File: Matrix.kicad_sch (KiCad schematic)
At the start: 139 parts, among them K1 esc, K10 9, K11 0, K12 -, K13 =, K15 backspace, K16 macro1, K17 tab, K18 q, K19 w, K2 1, K20 e, K21 r, K22 t, K23 y, K24 u, K25 i, K26 o, K27 p, K28 [, K29 ], K3 2, K30 \, K31 macro 2, K32 Caps, K33 a, K34 s, K35 d, K36 f, K37 g, K38 h, K39 j, K4 3, K40 k, K41 l, K42 ;, K43 ', K44 enter, K45 macro 3, K46 shift, K47 z, K48 x, K49 c, K5 4, K50 v, K51 b, K52 fn, K53 n, K54 m, K55 ,, K56 ., K57 /, K58 shift right, K59 up, K6 5, K60 ctrl left, K61 alt right, K62 space left, K63 code, K64 space right, K65 ctrl right, K66 left, K67 down, K68 right, K69 split backspace, K7 6, K70 space left 2, K71 code 2, K8 7, K9 8

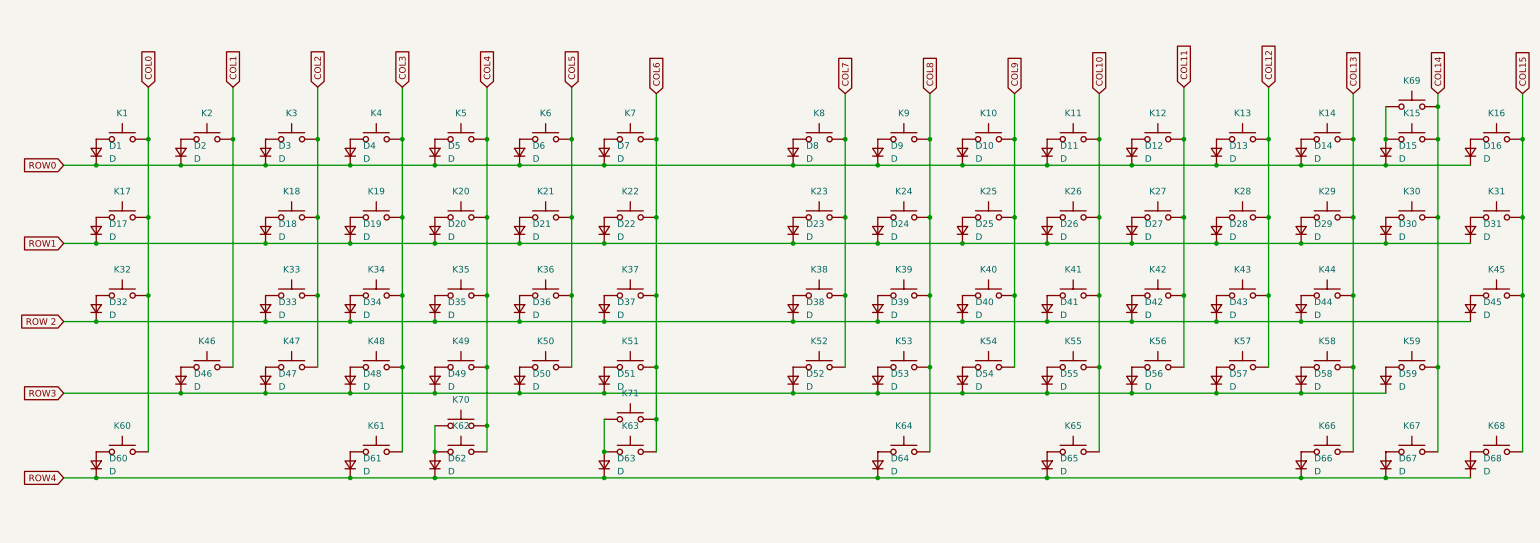
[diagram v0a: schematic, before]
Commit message: fixed footprint & Symbol
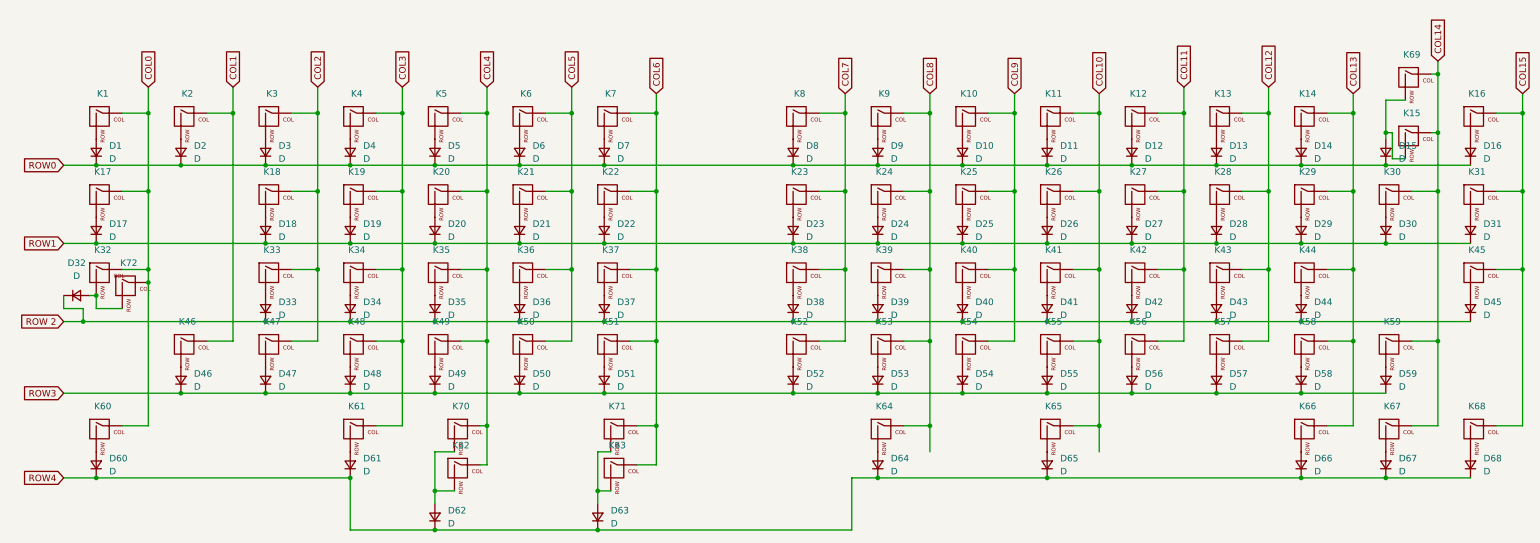
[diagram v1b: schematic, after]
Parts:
- added K72: Caps steped, Keyboard Component:SW_Cherry_MX_1.75u_PCB, symbol MX_Alps_Hybrid:MX-NoLED
- D1, D10, D11, D12, D13, D14, D15, D16, D17, D18, D19, D2, D20, D21, D22, D23, D24, D25, D26, D27, D28, D29, D3, D30, D31, D32, D33, D34, D35, D36, D37, D38, D39, D4, D40, D41, D42, D43, D44, D45, D46, D47, D48, D49, D5, D50, D51, D52, D53, D54, D55, D56, D57, D58, D59, D6, D60, D61, D62, D63, D64, D65, D66, D67, D68, D7, D8, D9: footprint (none) -> Diode_SMD:D_SOD-123
- K1, K10, K11, K12, K13, K14, K16, K18, K19, K2, K20, K21, K22, K23, K24, K25, K26, K27, K28, K29, K3, K31, K33, K34, K35, K36, K37, K38, K39, K4, K40, K41, K42, K43, K45, K47, K48, K49, K5, K50, K51, K52, K53, K54, K55, K56, K57, K59, K6, K63, K66, K67, K68, K7, K8, K9: footprint Button_Switch_Keyboard:SW_Cherry_MX_1.00u_PCB -> Keyboard Component:SW_Cherry_MX_1.00u_PCB; symbol Switch:SW_Push -> MX_Alps_Hybrid:MX-NoLED
- K15: value backspace -> split backspace; footprint Button_Switch_Keyboard:SW_Cherry_MX_1.00u_PCB -> Keyboard Component:SW_Cherry_MX_1.00u_PCB; symbol Switch:SW_Push -> MX_Alps_Hybrid:MX-NoLED
- K17, K30, K60, K61, K65: footprint Button_Switch_Keyboard:SW_Cherry_MX_1.00u_PCB -> Keyboard Component:SW_Cherry_MX_1.50u_PCB; symbol Switch:SW_Push -> MX_Alps_Hybrid:MX-NoLED
- K32, K58: footprint Button_Switch_Keyboard:SW_Cherry_MX_1.00u_PCB -> Keyboard Component:SW_Cherry_MX_1.75u_PCB; symbol Switch:SW_Push -> MX_Alps_Hybrid:MX-NoLED
- K44, K46, K62: footprint Button_Switch_Keyboard:SW_Cherry_MX_1.00u_PCB -> Keyboard Component:SW_Cherry_MX_2.25u_PCB; symbol Switch:SW_Push -> MX_Alps_Hybrid:MX-NoLED
- K64: footprint Button_Switch_Keyboard:SW_Cherry_MX_1.00u_PCB -> Keyboard Component:SW_Cherry_MX_2.75u_PCB; symbol Switch:SW_Push -> MX_Alps_Hybrid:MX-NoLED
- K69: value split backspace -> backspace; footprint Button_Switch_Keyboard:SW_Cherry_MX_1.00u_PCB -> Keyboard Component:SW_Cherry_MX_2.00u_PCB; symbol Switch:SW_Push -> MX_Alps_Hybrid:MX-NoLED
- K70: footprint Button_Switch_Keyboard:SW_Cherry_MX_1.00u_PCB -> Keyboard Component:SW_Cherry_MX_2.00u_PCB; symbol Switch:SW_Push -> MX_Alps_Hybrid:MX-NoLED
- K71: footprint Button_Switch_Keyboard:SW_Cherry_MX_1.00u_PCB -> Keyboard Component:SW_Cherry_MX_1.25u_PCB; symbol Switch:SW_Push -> MX_Alps_Hybrid:MX-NoLED
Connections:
- net COL0: now also K1.1 (COL), K17.1 (COL), K32.1 (COL), K60.1 (COL), K72.1 (COL); no longer K1.2, K17.2, K32.2, K60.2
- net COL1: now also K2.1 (COL), K46.1 (COL); no longer K2.2, K46.2
- net COL10: now also K11.1 (COL), K26.1 (COL), K41.1 (COL), K55.1 (COL), K65.1 (COL); no longer K11.2, K26.2, K41.2, K55.2, K65.2
- net COL11: now also K12.1 (COL), K27.1 (COL), K42.1 (COL), K56.1 (COL); no longer K12.2, K27.2, K42.2, K56.2
- net COL12: now also K13.1 (COL), K28.1 (COL), K43.1 (COL), K57.1 (COL); no longer K13.2, K28.2, K43.2, K57.2
- net COL13: now also K14.1 (COL), K29.1 (COL), K44.1 (COL), K58.1 (COL), K66.1 (COL); no longer K14.2, K29.2, K44.2, K58.2, K66.2
- net COL14: now also K15.1 (COL), K30.1 (COL), K59.1 (COL), K67.1 (COL), K69.1 (COL); no longer K15.2, K30.2, K59.2, K67.2, K69.2
- net COL15: now also K16.1 (COL), K31.1 (COL), K45.1 (COL), K68.1 (COL); no longer K16.2, K31.2, K45.2, K68.2
- net COL2: now also K18.1 (COL), K3.1 (COL), K33.1 (COL), K47.1 (COL); no longer K18.2, K3.2, K33.2, K47.2
- net COL3: now also K19.1 (COL), K34.1 (COL), K4.1 (COL), K48.1 (COL), K61.1 (COL); no longer K19.2, K34.2, K4.2, K48.2, K61.2
- net COL4: now also K20.1 (COL), K35.1 (COL), K49.1 (COL), K5.1 (COL), K62.1 (COL), K70.1 (COL); no longer K20.2, K35.2, K49.2, K5.2, K62.2, K70.2
- net COL5: now also K21.1 (COL), K36.1 (COL), K50.1 (COL), K6.1 (COL); no longer K21.2, K36.2, K50.2, K6.2
- net COL6: now also K22.1 (COL), K37.1 (COL), K51.1 (COL), K63.1 (COL), K7.1 (COL), K71.1 (COL); no longer K22.2, K37.2, K51.2, K63.2, K7.2, K71.2
- net COL7: now also K23.1 (COL), K38.1 (COL), K52.1 (COL), K8.1 (COL); no longer K23.2, K38.2, K52.2, K8.2
- net COL8: now also K24.1 (COL), K39.1 (COL), K53.1 (COL), K64.1 (COL), K9.1 (COL); no longer K24.2, K39.2, K53.2, K64.2, K9.2
- net COL9: now also K10.1 (COL), K25.1 (COL), K40.1 (COL), K54.1 (COL); no longer K10.2, K25.2, K40.2, K54.2
- net at D7.2 (A): now also K7.2 (ROW); no longer K7.1
- net at D2.2 (A): now also K2.2 (ROW); no longer K2.1
- net at D22.2 (A): now also K22.2 (ROW); no longer K22.1
- net at D31.2 (A): now also K31.2 (ROW); no longer K31.1
- net at D40.2 (A): now also K40.2 (ROW); no longer K40.1
- net at D9.2 (A): now also K9.2 (ROW); no longer K9.1
- net at D37.2 (A): now also K37.2 (ROW); no longer K37.1
- net at D48.2 (A): now also K48.2 (ROW); no longer K48.1
- net at D6.2 (A): now also K6.2 (ROW); no longer K6.1
- net at D57.2 (A): now also K57.2 (ROW); no longer K57.1
- net at D32.2 (A): now also K32.2 (ROW), K72.2 (ROW); no longer K32.1
- net at D65.2 (A): now also K65.2 (ROW); no longer K65.1
- net at D46.2 (A): now also K46.2 (ROW); no longer K46.1
- net at D44.2 (A): now also K44.2 (ROW); no longer K44.1
- net at D24.2 (A): now also K24.2 (ROW); no longer K24.1
- net at D45.2 (A): now also K45.2 (ROW); no longer K45.1
- net at D30.2 (A): now also K30.2 (ROW); no longer K30.1
- net at D16.2 (A): now also K16.2 (ROW); no longer K16.1
- net at D67.2 (A): now also K67.2 (ROW); no longer K67.1
- net at D13.2 (A): now also K13.2 (ROW); no longer K13.1
- net at D33.2 (A): now also K33.2 (ROW); no longer K33.1
- net at D56.2 (A): now also K56.2 (ROW); no longer K56.1
- net at D21.2 (A): now also K21.2 (ROW); no longer K21.1
- net at D29.2 (A): now also K29.2 (ROW); no longer K29.1
- net at D36.2 (A): now also K36.2 (ROW); no longer K36.1
- net at D42.2 (A): now also K42.2 (ROW); no longer K42.1
- net at D51.2 (A): now also K51.2 (ROW); no longer K51.1
- net at D53.2 (A): now also K53.2 (ROW); no longer K53.1
- net at D23.2 (A): now also K23.2 (ROW); no longer K23.1
- net at D39.2 (A): now also K39.2 (ROW); no longer K39.1
- net at D68.2 (A): now also K68.2 (ROW); no longer K68.1
- net at D19.2 (A): now also K19.2 (ROW); no longer K19.1
- net at D1.2 (A): now also K1.2 (ROW); no longer K1.1
- net at D52.2 (A): now also K52.2 (ROW); no longer K52.1
- net at D10.2 (A): now also K10.2 (ROW); no longer K10.1
- net at D64.2 (A): now also K64.2 (ROW); no longer K64.1
- net at D3.2 (A): now also K3.2 (ROW); no longer K3.1
- net at D55.2 (A): now also K55.2 (ROW); no longer K55.1
- net at D17.2 (A): now also K17.2 (ROW); no longer K17.1
- net at D60.2 (A): now also K60.2 (ROW); no longer K60.1
- net at D27.2 (A): now also K27.2 (ROW); no longer K27.1
- net at D28.2 (A): now also K28.2 (ROW); no longer K28.1
- net at D26.2 (A): now also K26.2 (ROW); no longer K26.1
- net at D66.2 (A): now also K66.2 (ROW); no longer K66.1
- net at D11.2 (A): now also K11.2 (ROW); no longer K11.1
- net at D59.2 (A): now also K59.2 (ROW); no longer K59.1
- net at D49.2 (A): now also K49.2 (ROW); no longer K49.1
- net at D43.2 (A): now also K43.2 (ROW); no longer K43.1
- net at D54.2 (A): now also K54.2 (ROW); no longer K54.1
- net at D34.2 (A): now also K34.2 (ROW); no longer K34.1
- net at D38.2 (A): now also K38.2 (ROW); no longer K38.1
- net at D35.2 (A): now also K35.2 (ROW); no longer K35.1
- net at D50.2 (A): now also K50.2 (ROW); no longer K50.1
- net at D41.2 (A): now also K41.2 (ROW); no longer K41.1
- net at D12.2 (A): now also K12.2 (ROW); no longer K12.1
- net at D5.2 (A): now also K5.2 (ROW); no longer K5.1
- net at D61.2 (A): now also K61.2 (ROW); no longer K61.1
- net at D58.2 (A): now also K58.2 (ROW); no longer K58.1
- net at D20.2 (A): now also K20.2 (ROW); no longer K20.1
- net at D14.2 (A): now also K14.2 (ROW); no longer K14.1
- net at D47.2 (A): now also K47.2 (ROW); no longer K47.1
- net at D4.2 (A): now also K4.2 (ROW); no longer K4.1
- net at D25.2 (A): now also K25.2 (ROW); no longer K25.1
- net at D8.2 (A): now also K8.2 (ROW); no longer K8.1
- net at D18.2 (A): now also K18.2 (ROW); no longer K18.1
- new net: D63.2 (A), K63.2 (ROW), K71.2 (ROW)
- new net: D62.2 (A), K62.2 (ROW), K70.2 (ROW)
- new net: D15.2 (A), K15.2 (ROW), K69.2 (ROW)
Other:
- moved on the sheet: D32, D62, D63
